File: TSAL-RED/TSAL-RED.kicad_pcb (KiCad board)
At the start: 2 copper layers, 47 parts, among them J1 Conn_01x02, J2 Conn_01x02, K1 G5V-2, Q1 2N7002, Q2 IRF9540N, U1 LM358, U2 4N35, U3 NE555D

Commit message: CREATE TSAL PCBs
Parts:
- removed R24, R25: 100, Resistor_SMD:R_2512_6332Metric_Pad1.40x3.35mm_HandSolder
- added D4: GRN, LED_SMD:LED_0805_2012Metric_Pad1.15x1.40mm_HandSolder, F.Cu at (126.1, 74.5)
- added G***: LOGO, LOGO, F.Cu at (70.0, 62.6)
- added J3: Conn_02x01, Connector_Molex:Molex_Micro-Fit_3.0_43045-0212_2x01_P3.00mm_Vertical, F.Cu at (127.0, 101.4)
- added J4: Conn_02x01, Connector_Molex:Molex_Micro-Fit_3.0_43045-0212_2x01_P3.00mm_Vertical, F.Cu at (126.9, 107.5)
- added J5: Conn_02x01, Connector_Molex:Molex_Micro-Fit_3.0_43045-0212_2x01_P3.00mm_Vertical, F.Cu at (117.3, 107.4)
- added R29: 2k2, Resistor_SMD:R_0603_1608Metric_Pad0.98x0.95mm_HandSolder, F.Cu at (126.1, 70.5)
- added REF**: Symbol_HighVoltage_Triangle_6x6mm_Copper, Symbol:Symbol_HighVoltage_Triangle_6x6mm_Copper, F.Cu at (90.1, 76.1)
- J1, J2: footprint Connector_Molex:Molex_Micro-Fit_3.0_43650-0215_1x02_P3.00mm_Vertical -> Connector_Molex:Molex_Mini-Fit_Jr_5566-02A_2x01_P4.20mm_Vertical
- Q2: value IRF9540N -> AO3401A; footprint Package_TO_SOT_THT:TO-220-4_Horizontal_TabDown -> Package_TO_SOT_SMD:SOT-23
- R10, R11, R7, R8, R9: footprint Resistor_SMD:R_0201_0603Metric_Pad0.64x0.40mm_HandSolder -> Resistor_SMD:R_0603_1608Metric_Pad0.98x0.95mm_HandSolder
- R28: value 330 -> 910
- moved R18 86.0 mm to (59.0, 73.5)
- moved R21 85.9 mm to (58.9, 91.1)
- moved R19 85.1 mm to (83.3, 108.9)
- moved R4 83.9 mm to (79.4, 115.5)
- moved R14 79.5 mm to (79.4, 109.0), turned to 180 degrees
- moved R23 76.4 mm to (58.9, 85.2)
- moved R22 75.7 mm to (79.2, 79.3), turned to 180 degrees
- moved R20 74.9 mm to (79.2, 97.0), turned to 180 degrees
- moved H2 73.6 mm to (54.2, 117.6)
- moved R26 72.9 mm to (100.8, 76.4), turned to 180 degrees
- moved R1 72.2 mm to (89.3, 87.9), turned to -90 degrees
- moved R17 71.9 mm to (58.9, 103.0)
- moved C4 71.3 mm to (102.3, 74.4), turned to 180 degrees
- moved R2 68.9 mm to (92.2, 87.9), turned to -90 degrees
- moved U1 68.5 mm to (98.3, 86.9)
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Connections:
- U1 pad 2: /Vref -> /Vin
- U1 pad 3: /Vin -> /Vref
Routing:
- net GLV+: track 0.00 -> 72.0 mm
- net TS+: track 0.00 -> 59.2 mm
- net TS-: track 0.00 -> 44.8 mm, vias 0 -> 198
- net /GRN+: track 0.00 -> 38.7 mm
- net /RED+: track 0.00 -> 38.5 mm
- net /5V+_Iso: track 0.00 -> 25.9 mm
- net Net-(R15-Pad2): track 0.00 -> 16.9 mm
- net Net-(J2-Pin_1): track 0.00 -> 15.9 mm
- net Net-(K1-Pad13): track 0.00 -> 15.4 mm
- net /Vref: track 0.00 -> 14.4 mm
- net Net-(U3-THR): track 0.00 -> 10.1 mm
- net Net-(J2-Pin_2): track 0.00 -> 9.66 mm
- net Net-(Q2-G): track 0.00 -> 9.38 mm
- net Net-(Q1-D): track 0.00 -> 8.77 mm
- net Net-(R3-Pad2): track 0.00 -> 7.35 mm, vias 0 -> 1
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- added copper zone on B.Cu, net /5V-_Iso
- added copper zone on F.Cu, net /5V-_Iso
- added copper zone on B.Cu, net GLV-
- added copper zone on F.Cu, net GLV-
- added copper zone on B.Cu, net TS-
- added copper zone on F.Cu, net TS-
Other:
- board outline added: 84 x 62.5 mm
- board text added: "+ -"
- board text added: "0.2000 mm / 0.2000 mm"
- board text added: "0.3000 mm"
- board text added: "1.6000 mm"
- board text added: "2"
- board text added: "84.0000 mm x 62.5000 mm"
- board text added: "BOARD CHARACTERISTICS"
- board text added: "Board Thickness:"
- board text added: "Board overall dimensions:"
- board text added: "Castellated pads:"
- board text added: "Copper Finish:"
- board text added: "Copper Layer Count:"
- board text added: "Edge card connectors:"
- board text added: "FLY SAFE!"
- board text added: "G In"
- board text added: "GRN"
- board text added: "HAL SnPb"
- board text added: "HIGH VOLTAGE"
- board text added: "HV LV"
- board text added: "Impedance Control:"
- board text added: "Min hole diameter:"
- board text added: "Min track/spacing:"
- board text added: "No"
- board text added: "Plated Board Edge:"
- board text added: "R+ G+"
- board text added: "RED"
- board text added: "TS"
- board text added: "TSMP"
- board text added: "V1.0"

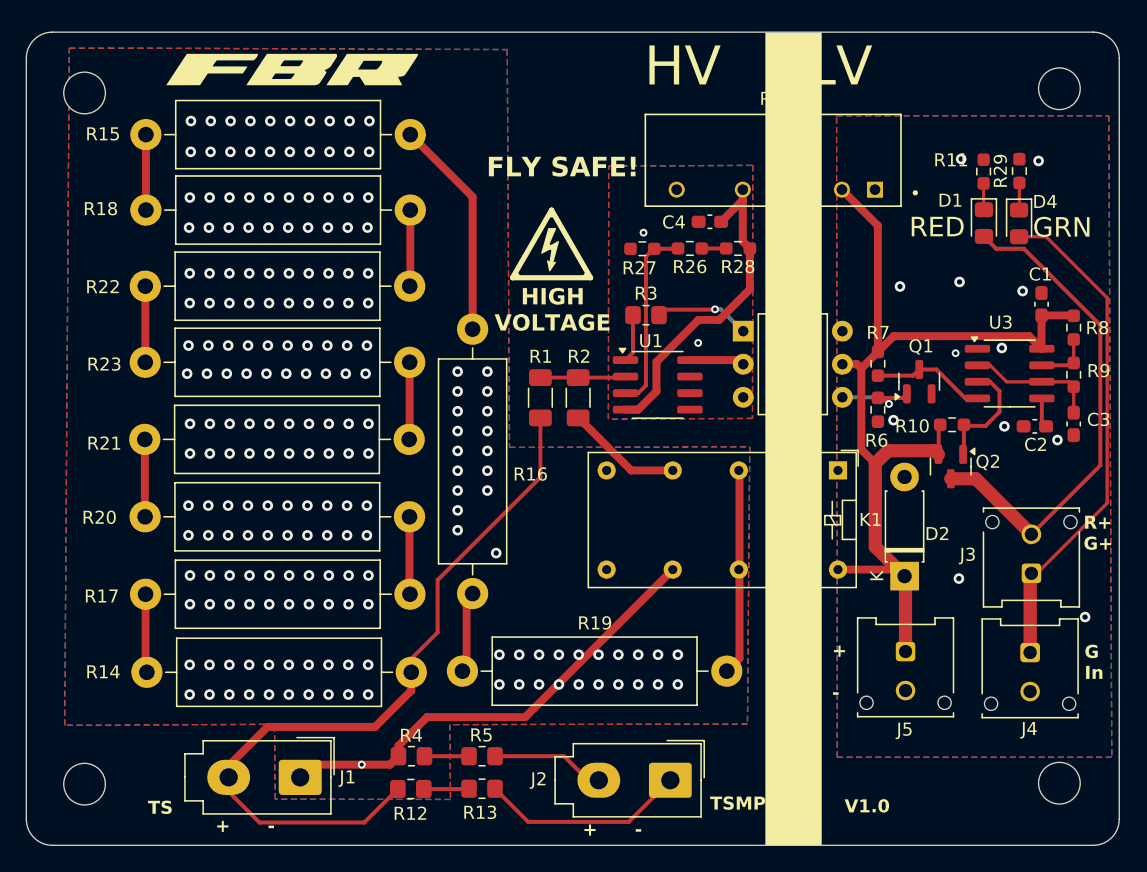
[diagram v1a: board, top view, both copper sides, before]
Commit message: Modify TSAL PCB and use relative paths for libraries
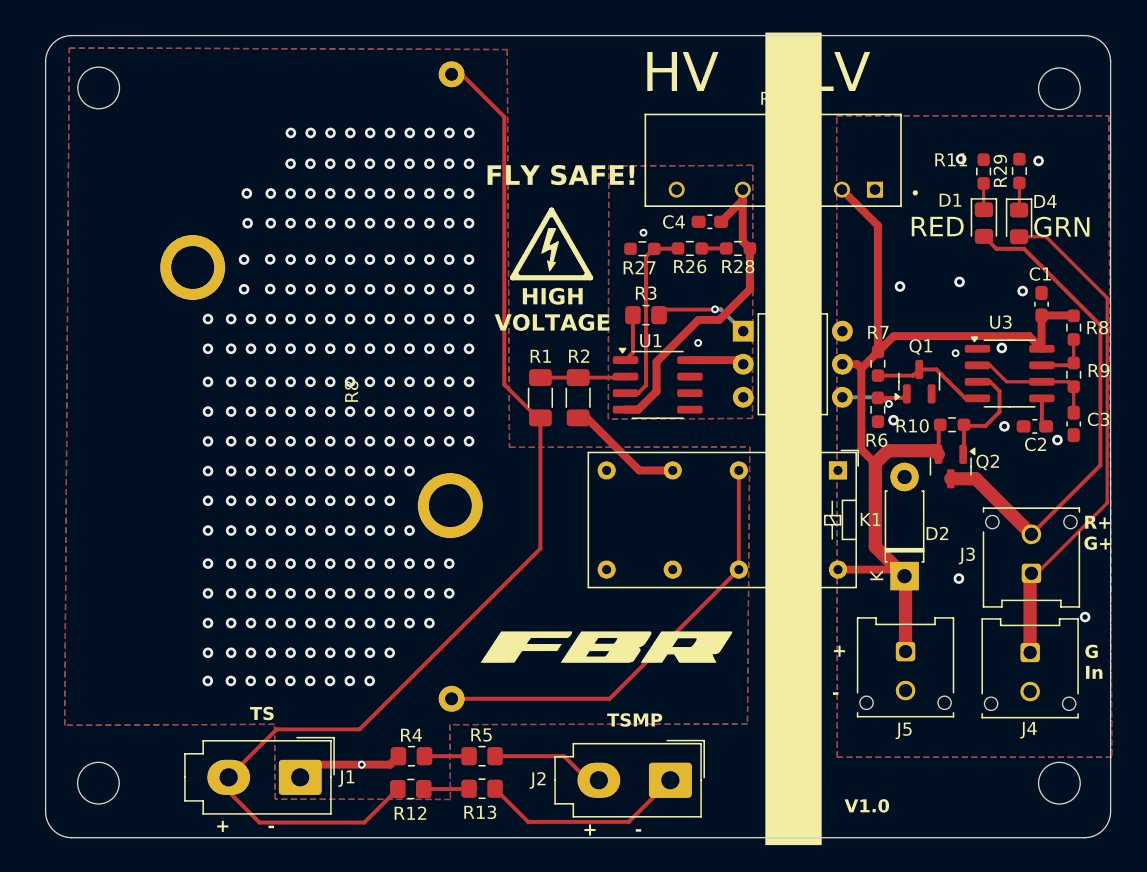
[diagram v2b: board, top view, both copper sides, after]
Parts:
- removed R15, R16, R17, R18, R19, R20, R21, R22, R23: 120, Resistor_THT:R_Axial_DIN0516_L15.5mm_D5.0mm_P20.32mm_Horizontal
- R14: value 120 -> 1.2K; footprint Resistor_THT:R_Axial_DIN0516_L15.5mm_D5.0mm_P20.32mm_Horizontal -> Chassis_Resistor:HSA25
- moved G*** 50.5 mm to (94.2, 107.0)
- moved R14 23.0 mm to (72.5, 87.0), turned to 90 degrees
- moved H1 1.15 mm to (55.3, 64.1)
- moved H2 1.07 mm to (55.3, 117.5)
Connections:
- R14 pad 2: Net-(R14-Pad2) -> Net-(K1-Pad13)
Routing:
- net TS+: track 59.2 -> 88.8 mm
- net TS-: track 44.8 -> 17.3 mm, vias 198 -> 228
- net Net-(K1-Pad13): track 15.4 -> 33.9 mm
- net Net-(R15-Pad2): track 16.9 -> 0.00 mm
- net Net-(R16-Pad2): track 6.73 -> 0.00 mm
- net Net-(R14-Pad2): track 6.04 -> 0.00 mm
- net Net-(R17-Pad2): track 5.96 -> 0.00 mm
- net Net-(R20-Pad2): track 5.96 -> 0.00 mm
- net Net-(R21-Pad2): track 5.94 -> 0.00 mm
- net Net-(R18-Pad2): track 5.87 -> 0.00 mm
- net Net-(R22-Pad2): track 5.85 -> 0.00 mm
- net Net-(R15-Pad1): track 5.80 -> 0.00 mm
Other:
- board size 84 x 62.5 mm -> 81.9 x 61.6 mm
- board text added: "150"
- board text added: "R8"

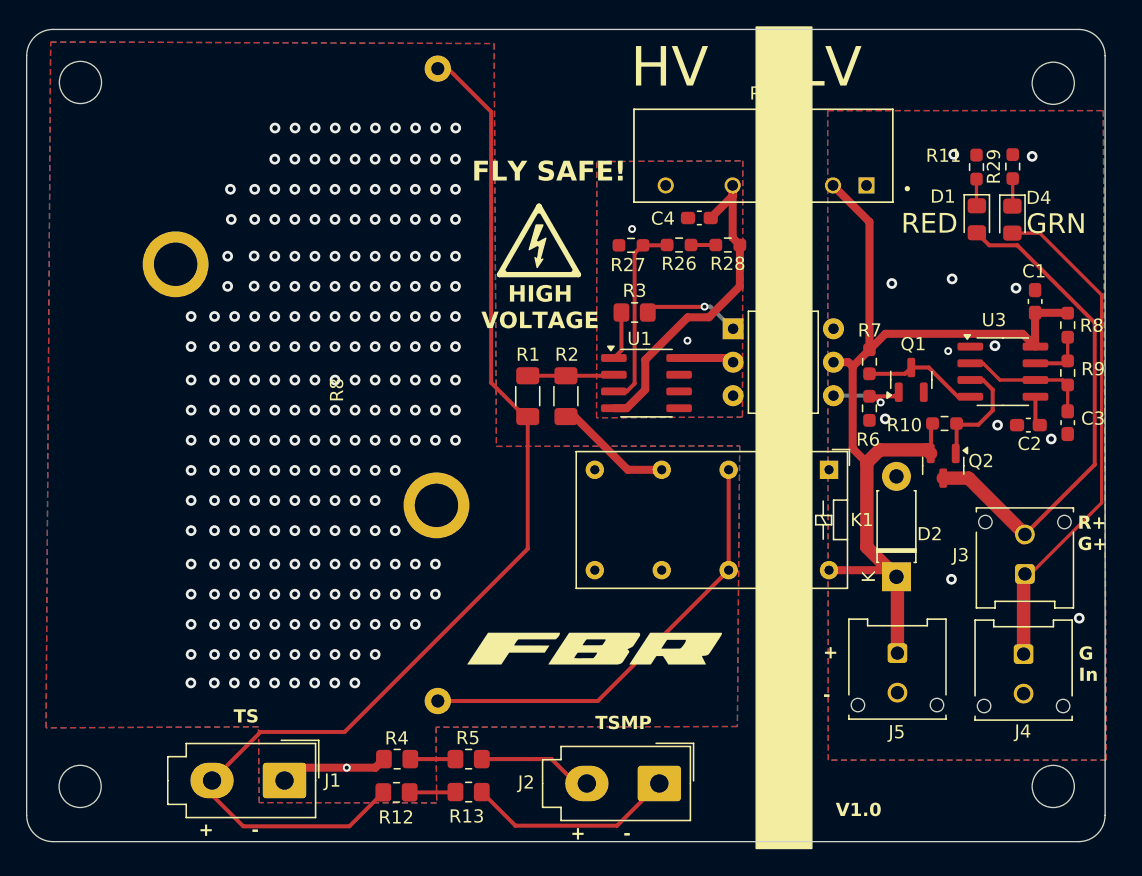
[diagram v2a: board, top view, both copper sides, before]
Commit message: Single signal connector
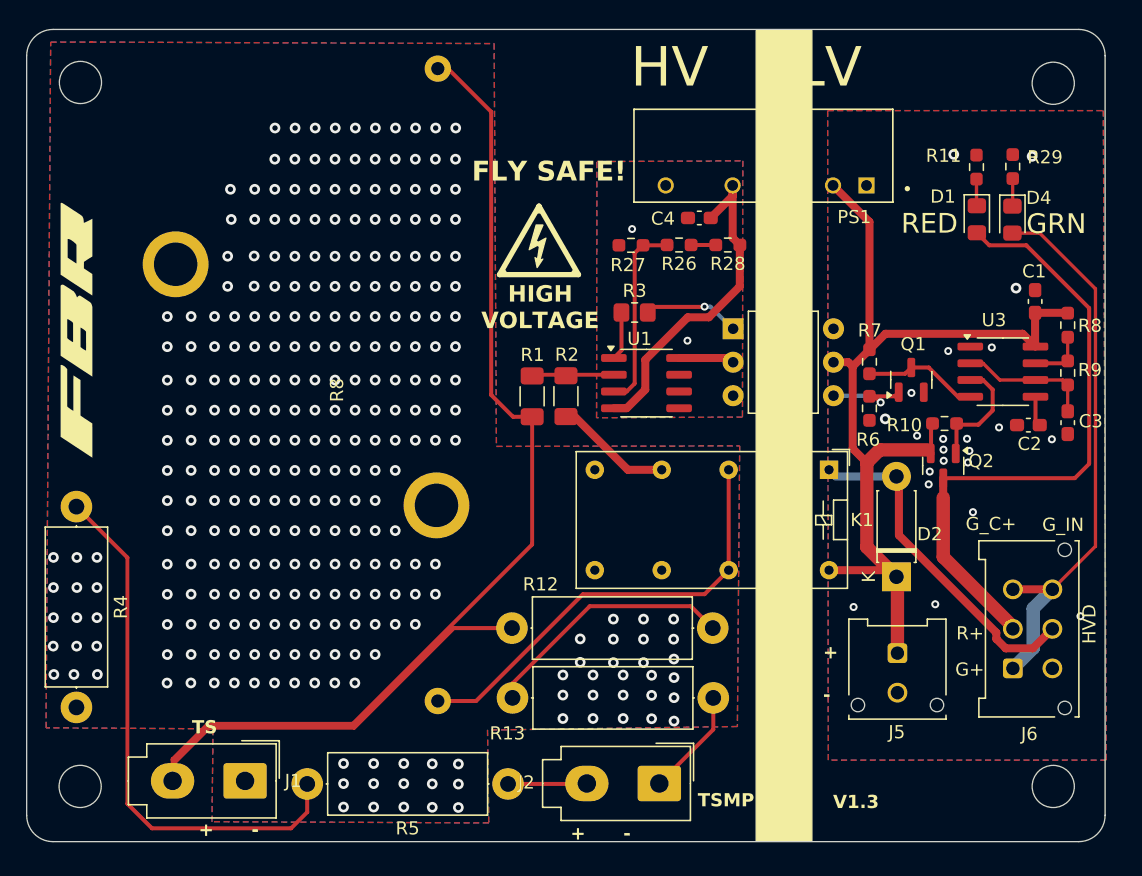
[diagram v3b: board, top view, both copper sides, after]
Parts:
- removed J3, J4: Conn_02x01, Connector_Molex:Molex_Micro-Fit_3.0_43045-0212_2x01_P3.00mm_Vertical
- added J6: Conn_02x03_Counter_Clockwise, Connector_Molex:Molex_Micro-Fit_3.0_43045-0612_2x03_P3.00mm_Vertical, F.Cu at (126.1, 108.6)
- R12, R4: value 4.7K -> 2.2K; footprint Resistor_SMD:R_0805_2012Metric_Pad1.20x1.40mm_HandSolder -> Resistor_THT:R_Axial_DIN0414_L11.9mm_D4.5mm_P15.24mm_Horizontal
- R13, R5: value 270 -> 2.7K; footprint Resistor_SMD:R_0805_2012Metric_Pad1.20x1.40mm_HandSolder -> Resistor_THT:R_Axial_DIN0414_L11.9mm_D4.5mm_P15.24mm_Horizontal
- moved G*** 46.0 mm to (55.0, 83.1), turned to 90 degrees
- moved R4 31.0 mm to (55.0, 96.3), turned to -90 degrees
- moved R12 27.1 mm to (103.3, 105.5)
- moved R13 19.9 mm to (103.4, 110.8)
- moved R5 3.53 mm to (87.8, 117.3), turned to 180 degrees
- moved J1 2.99 mm to (67.8, 117.1)
- moved R1 0.34 mm to (89.6, 87.9)
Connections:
- D2 pad 2: GLV- -> HVD_SDC_IN
- K1 pad 1: GLV- -> HVD_SDC_IN
- R4 pad 1: TS- -> Net-(R4-Pad1)
- R4 pad 2: Net-(R4-Pad2) -> TS-
- R5 pad 1: Net-(R4-Pad2) -> Net-(J2-Pin_2)
- R5 pad 2: Net-(J2-Pin_2) -> Net-(R4-Pad1)
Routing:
- net Net-(R4-Pad1): track 0.00 -> 41.2 mm
- net HVD_SDC_IN: track 0.00 -> 26.0 mm
- net TS+: track 88.8 -> 108.2 mm
- net Net-(R12-Pad1): track 3.49 -> 19.4 mm
- net /RED+: track 38.5 -> 48.3 mm
- net TS-: track 17.3 -> 9.07 mm, vias 228 -> 296
- net Net-(J2-Pin_1): track 15.9 -> 8.19 mm
- net /GRN+: track 38.7 -> 42.5 mm
- net Net-(R4-Pad2): track 3.42 -> 0.00 mm
- net Net-(J2-Pin_2): track 9.66 -> 7.74 mm
- net Net-(K1-Pad13): track 33.9 -> 34.4 mm
- net GLV-: vias 12 -> 22
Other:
- board text added: "81.8560 mm x 61.6500 mm"
- board text added: "G+"
- board text added: "G_C+"
- board text added: "G_IN"
- board text added: "HVD"
- board text added: "R+"
- board text added: "V1.3"
- board text removed: "84.0000 mm x 62.5000 mm"
- board text removed: "G In"
- board text removed: "R+ G+"
- board text removed: "V1.0"

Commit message: update check
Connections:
- J6 pad 4: unconnected-(J6-Pin_4-Pad4) -> GLV-
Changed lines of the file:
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@@
 	(net 30 "Net-(R4-Pad1)")
 	(net 31 "HVD_SDC_IN")
-	(net 32 "unconnected-(J6-Pin_4-Pad4)")
 	(footprint "Diode_THT:D_DO-41_SOD81_P7.62mm_Horizontal"
 		(layer "F.Cu")
@@
 			(layers "*.Cu" "*.Mask")
 			(remove_unused_layers no)
-			(net 32 "unconnected-(J6-Pin_4-Pad4)")
+			(net 1 "GLV-")
 			(pinfunction "Pin_4")
-			(pintype "passive+no_connect")
+			(pintype "passive")
 		)
 		(pad "5" thru_hole circle
@@
 	)
 	(segment
-		(start 125.570786 107.044214)
-		(end 127.630786 107.044214)
+		(start 124.528786 105.522214)
+		(end 124.528786 106.002214)
 		(width 0.6096)
 		(layer "F.Cu")
@@
 	(segment
 		(start 117.460786 98.454214)
-		(end 124.855986 105.849414)
+		(end 124.528786 105.522214)
 		(width 0.6096)
 		(layer "F.Cu")
@@
 	)
 	(segment
-		(start 117.460786 94.175786)
-		(end 117.460786 98.454214)
+		(start 124.528786 106.002214)
+		(end 125.570786 107.044214)
 		(width 0.6096)
 		(layer "F.Cu")
@@
 	)
 	(segment
-		(start 117.275 93.99)
-		(end 117.460786 94.175786)
+		(start 117.460786 94.175786)
+		(end 117.460786 98.454214)
 		(width 0.6096)
 		(layer "F.Cu")
@@
 	)
 	(segment
-		(start 124.855986 105.849414)
-		(end 124.855986 106.329414)
+		(start 125.570786 107.044214)
+		(end 127.630786 107.044214)
 		(width 0.6096)
 		(layer "F.Cu")
@@
 	)
 	(segment
-		(start 124.855986 106.329414)
-		(end 125.570786 107.044214)
+		(start 117.275 93.99)
+		(end 117.460786 94.175786)
 		(width 0.6096)
 		(layer "F.Cu")
